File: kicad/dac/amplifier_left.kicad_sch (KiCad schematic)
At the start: 29 parts, among them Q2 PNP, Q3 PNP, Q4 NPN, Q5 NPN, Q6 NPN, Q7 PNP, Q8 NPN, Q9 PNP

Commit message: split power supply to different board
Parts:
- removed HS1: Heatsink_Pad, symbol Mechanical:Heatsink_Pad
- added HS1: Heatsink, Heatsink:Heatsink_Fischer_SK104-STCB_35x13mm__2xDrill3.5mm_ScrewM3, symbol Mechanical:Heatsink
- C12: value 750n -> 1u
- Q4: footprint (none) -> Package_TO_SOT_THT:TO-92L_Inline
- Q8, Q9: footprint (none) -> Package_TO_SOT_THT:TO-220-3_Vertical
- R15: value 1k -> 870
- RV1: footprint (none) -> library:RK09L12B
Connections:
- net IN_L renamed IN
- net OUT_L renamed OUT

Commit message: Commit
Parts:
- removed C12: 1u, symbol Device:C
- removed I1: 2mA, symbol Simulation_SPICE:IDC
- removed I2: 10mA, symbol Simulation_SPICE:IDC
- removed Q2, Q3: PNP, symbol Simulation_SPICE:PNP
- removed Q5: NPN, symbol Simulation_SPICE:NPN
- removed R15: 870, Resistor_THT:R_Axial_DIN0207_L6.3mm_D2.5mm_P10.16mm_Horizontal, symbol Device:R
- removed R19: 22, Resistor_THT:R_Axial_DIN0207_L6.3mm_D2.5mm_P10.16mm_Horizontal, symbol Device:R
- removed R20, R21: 33, Resistor_THT:R_Axial_DIN0207_L6.3mm_D2.5mm_P10.16mm_Horizontal, symbol Device:R
- removed R22, R23: 330m, symbol Device:R
- added C11: 120p, symbol Device:C
- added C20: 10u, Capacitor_THT:CP_Radial_D5.0mm_P2.50mm, symbol Device:C_Polarized
- added C21, C22: 10u, symbol Device:C
- added C23, C24: 100u, symbol Device:C_Polarized
- added Q10: NPN, Package_SO:SC-74-6_1.5x2.9mm_P0.95mm, symbol library:Dual-NPN
- added Q12, Q8: PNP, Package_SO:SC-74-6_1.5x2.9mm_P0.95mm, symbol library:Dual-PNP
- added Q4 (x2): NPN, Package_TO_SOT_THT:TO-92, symbol Simulation_SPICE:NPN
- added unit 2 of Q8
- added unit 2 of Q9
- added R12: 470, Resistor_SMD:R_1206_3216Metric_Pad1.30x1.75mm_HandSolder, symbol Device:R
- added R13: 68, Resistor_THT:R_Axial_DIN0207_L6.3mm_D2.5mm_P10.16mm_Horizontal, symbol Device:R
- added R13 (x2), R15: 68, Resistor_SMD:R_1206_3216Metric_Pad1.30x1.75mm_HandSolder, symbol Device:R
- added R15: 680, Resistor_SMD:R_1206_3216Metric_Pad1.30x1.75mm_HandSolder, symbol Device:R
- added R15 (x2): 27k, Resistor_SMD:R_1206_3216Metric_Pad1.30x1.75mm_HandSolder, symbol Device:R
- added R19: 22, Resistor_SMD:R_1206_3216Metric_Pad1.30x1.75mm_HandSolder, symbol Device:R
- added R19: 2k2, Resistor_SMD:R_1206_3216Metric_Pad1.30x1.75mm_HandSolder, symbol Device:R
- added R20 (x2): 33, Resistor_SMD:R_1206_3216Metric_Pad1.30x1.75mm_HandSolder, symbol Device:R
- added R38: 500, symbol Device:R_Trim
- added R40: 100, Resistor_SMD:R_1206_3216Metric_Pad1.30x1.75mm_HandSolder, symbol Device:R
- added R9 (x2): 1, Resistor_THT:R_Axial_DIN0614_L14.3mm_D5.7mm_P20.32mm_Horizontal, symbol Device:R
- added RV2: 100, symbol Device:R_Potentiometer_Trim
- C10: footprint (none) -> Capacitor_SMD:C_1206_3216Metric_Pad1.33x1.80mm_HandSolder
- C7: value 1n -> 2u2
- HS1: footprint Heatsink:Heatsink_Fischer_SK104-STCB_35x13mm__2xDrill3.5mm_ScrewM3 -> Heatsink:Heatsink_Fischer_SK129-STS_42x25mm_2xDrill2.5mm; Digikey (none) -> HS404-ND; DigikeyAlt (none) -> FA-T220-25E-ND; Height (none) -> 25.4mm
- Q4: footprint Package_TO_SOT_THT:TO-92L_Inline -> Package_TO_SOT_THT:TO-92
- R12: value 1k -> 470; footprint Resistor_THT:R_Axial_DIN0207_L6.3mm_D2.5mm_P10.16mm_Horizontal -> Resistor_SMD:R_1206_3216Metric_Pad1.30x1.75mm_HandSolder
- R13, R14: value 234 -> 430; footprint Resistor_THT:R_Axial_DIN0207_L6.3mm_D2.5mm_P10.16mm_Horizontal -> Resistor_SMD:R_1206_3216Metric_Pad1.30x1.75mm_HandSolder
- R15: value 1k -> 2k
- R16: value 10k -> 20k
- R17: value 1k2 -> 2k2; footprint Resistor_THT:R_Axial_DIN0207_L6.3mm_D2.5mm_P10.16mm_Horizontal -> Resistor_SMD:R_1206_3216Metric_Pad1.30x1.75mm_HandSolder
- R18: value 518 -> 680; footprint Resistor_THT:R_Axial_DIN0207_L6.3mm_D2.5mm_P10.16mm_Horizontal -> Resistor_SMD:R_1206_3216Metric_Pad1.30x1.75mm_HandSolder
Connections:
- net GNDA: now also C11.2, C21.2, C22.1, C23.2, C24.1, Q4.1 (C), R15.1, R15.1
- net IN: now also R13.1; no longer RV1.1
- net OUT: now also R20.1, R20.2, R9.1, R9.2
- net at R12.2: now also Q10.5 (E); no longer C10.1
- net at C10.2, Q4.3 (E), Q7.2 (B): now also C20.2, Q4.1 (C), R38.2; no longer R18.1
- net at R13.2: now also R13.1, RV2.1; no longer R14.1
- net at C7.2, R11.2: now also Q8.1 (B)
- net at R13.1: now also Q8.5 (E)
- net at Q8.3 (E): now also R9.1
- net at Q7.3 (E), Q9.2 (B): now also R20.1
- net at R15.2, R16.1: now also Q8.2 (B)
- net at Q6.3 (E), Q8.2 (B): now also R20.2
- net at R14.2: now also Q8.4 (E)
- net at Q4.1 (C), Q6.2 (B): now also C20.1, R40.2; no longer R17.2
- net at Q9.3 (E): now also R9.2
- net +36V renamed +30V
- net +30V: now also C21.1, C23.1, Q12.5 (E), Q9.5 (E), R15.2, R15.2
- net -36V renamed -30V
- net -30V: now also C22.2, C24.2, R12.1, R19.1, R19.1
- new net: Q12.3 (C), R17.2, R40.1
- new net: R18.1, R38.1
- new net: Q4.2 (B), Q4.3 (E), R19.2
- new net: Q4.3 (E), R19.2
- new net: C11.1, R13.2, RV1.1
- new net: C10.1, Q10.6 (C), Q4.2 (B), Q8.6 (C)
- new net: R13.1, R14.1, RV2.3
- new net: Q10.1 (B), Q10.2 (B), Q10.3 (C), Q8.3 (C)
- new net: Q9.2 (B), Q9.6 (C), R15.2
- new net: Q9.3 (C), R13.2, R13.2, RV2.2
- new net: Q9.1 (B), Q9.4 (E), R15.1
- new net: Q10.4 (E), R12.2
- new net: Q12.2 (B), Q12.6 (C), R15.2
- new net: Q12.1 (B), Q12.4 (E), R15.1
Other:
- note added: "0.5mA"
- note added: "1.7V above V-"
- note added: "10mA"
- note added: "1mA"
- note added: "=Vbe factor * re'"
- note added: "Iq=26mA"
- note added: "MASTER"
- note added: "This sheet for the left channel amplifier is where design changes happen. Afterwards its design is copied to the right channel amplifier. Beware of potentiometer A/B variants. All resistors are 1/4W 1206 unless specified."
- note added: "Vbias=4*Vbe"
- note added: "best transistors: input: ultra low noise, low Cob, well matched vas: first part: fT >> 100MHz @ Ic, low noise vas: last part: fT >> 100MHz @ Ic, small Early effect, low Cob output: first part: low Cob output: last part: big SOA"
- note added: "wire wound: galaxy brain metal thin film: yeah boi carbon film: good metal thick film: meh metal oxide film: trash carbon composition: trash"
- title: USB DAC & Headphone Amplifier -> Left Channel Amplifier
- moved on the sheet: C10, C7, HS1, Q4, R11, R12, R13, R14, R15, R16, R17, R18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

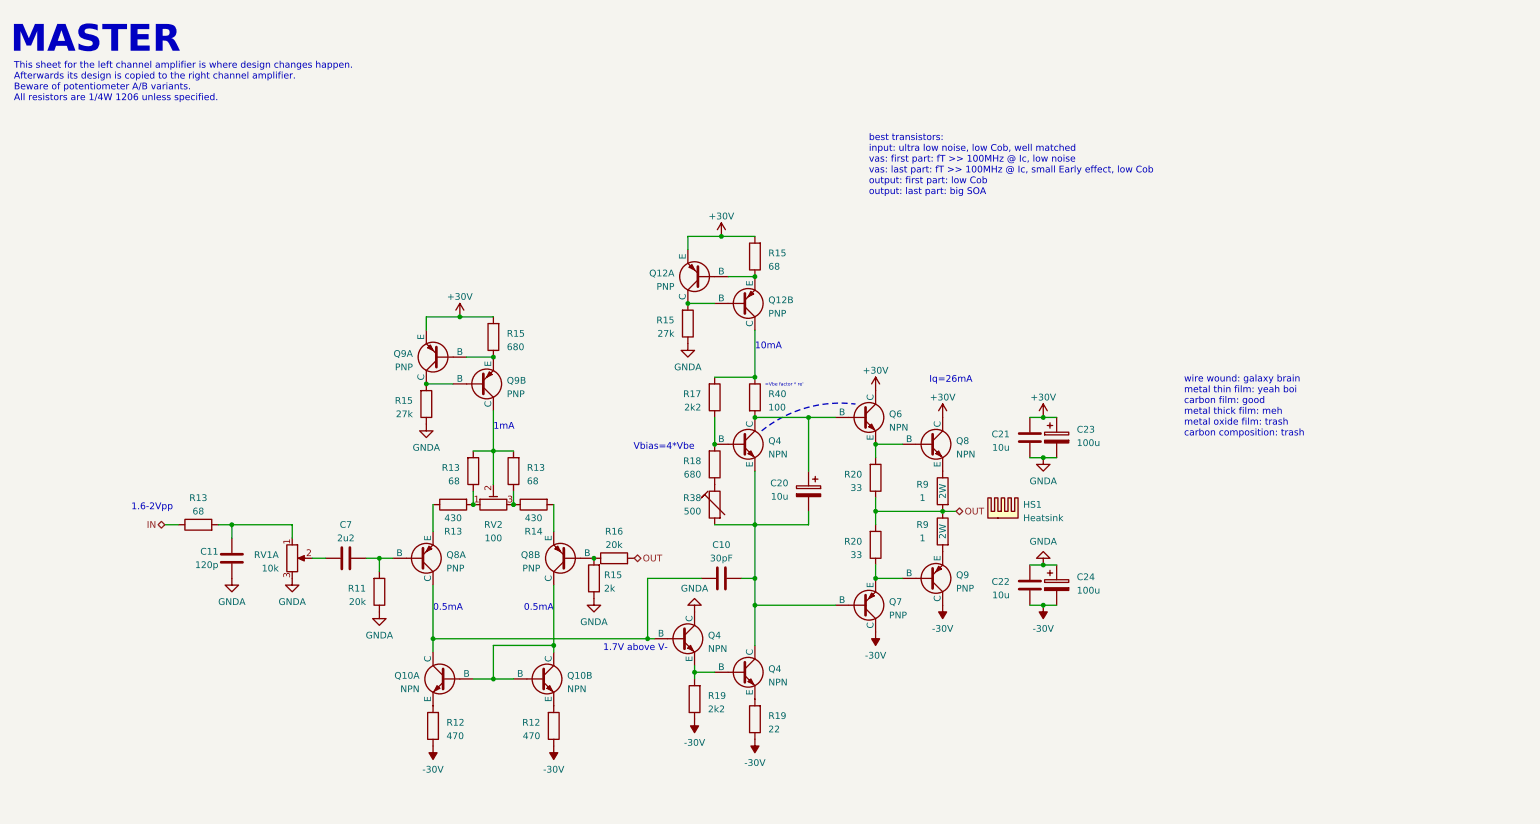
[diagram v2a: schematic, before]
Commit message: completed power supply footprints and placement
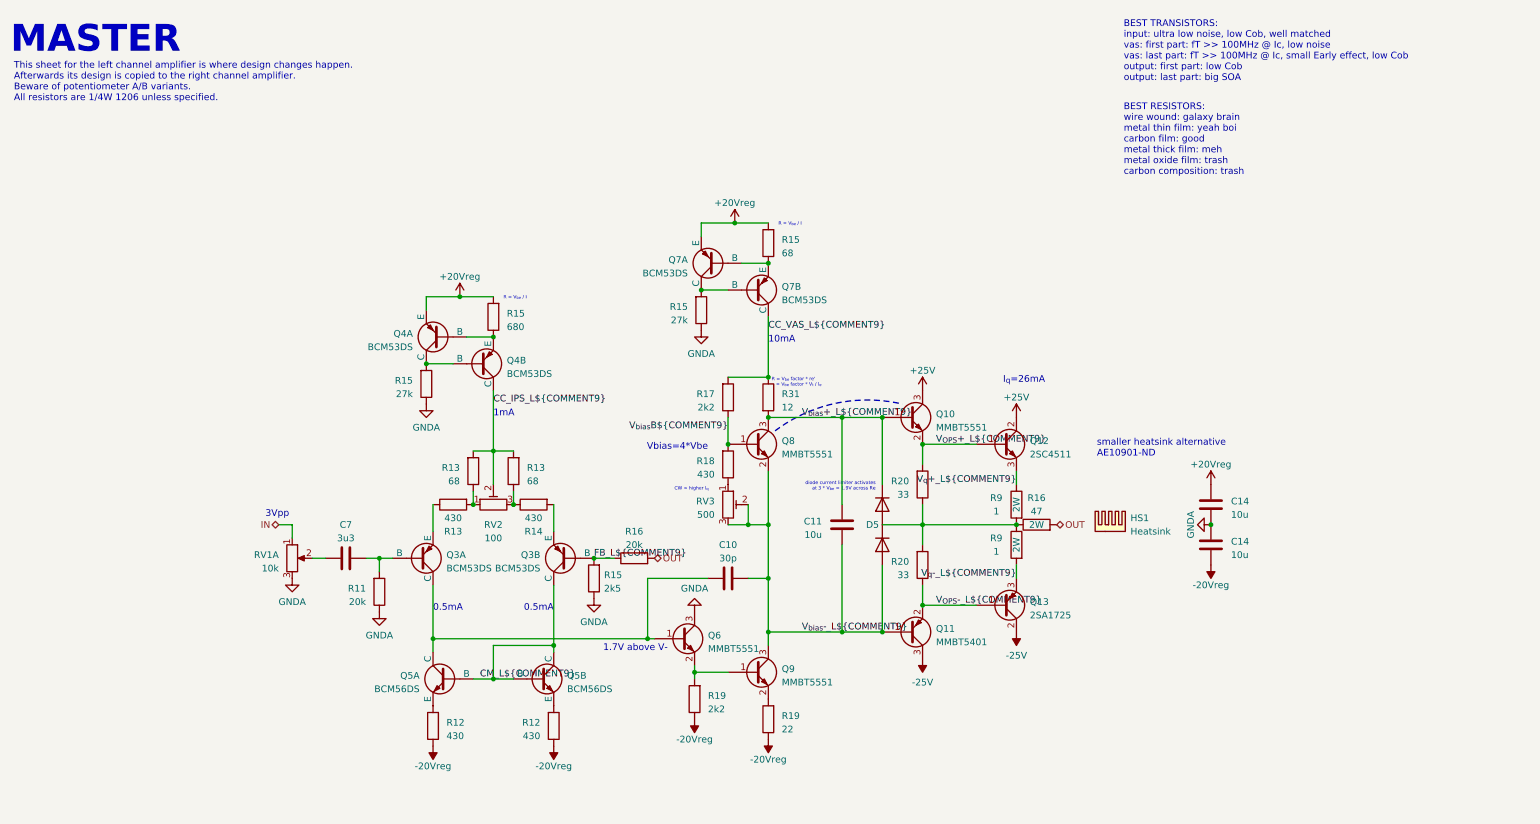
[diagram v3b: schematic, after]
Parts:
- removed C20: 10u, Capacitor_THT:CP_Radial_D5.0mm_P2.50mm, symbol Device:C_Polarized
- removed C21, C22: 10u, symbol Device:C
- removed C23, C24: 100u, symbol Device:C_Polarized
- removed Q4 (x3): NPN, Package_TO_SOT_THT:TO-92, symbol Simulation_SPICE:NPN
- removed Q6: NPN, symbol Simulation_SPICE:NPN
- removed Q7: PNP, symbol Simulation_SPICE:PNP
- removed Q8: NPN, Package_TO_SOT_THT:TO-220-3_Vertical, symbol Simulation_SPICE:NPN
- removed Q9: PNP, Package_TO_SOT_THT:TO-220-3_Vertical, symbol Simulation_SPICE:PNP
- removed R13: 68, Resistor_THT:R_Axial_DIN0207_L6.3mm_D2.5mm_P10.16mm_Horizontal, symbol Device:R
- removed R38: 500, symbol Device:R_Trim
- added C14 (x2): 10u, Capacitor_SMD:C_1206_3216Metric_Pad1.33x1.80mm_HandSolder, symbol Device:C
- added D5: ~, Package_TO_SOT_SMD:SOT-23-3, symbol library:Dual_Diode_Array
- added Q10, Q6, Q8, Q9: MMBT5551, Package_TO_SOT_SMD:SOT-23-3, symbol Device:Q_NPN_BEC
- added Q11: MMBT5401, Package_TO_SOT_SMD:SOT-23-3, symbol Device:Q_PNP_BEC
- added Q12: 2SC4511, Package_TO_SOT_THT:TO-220F-3_Vertical, symbol Device:Q_NPN_BCE
- added Q13: 2SA1725, Package_TO_SOT_THT:TO-220F-3_Vertical, symbol Device:Q_PNP_BCE
- added R16: 47, symbol Device:R
- added RV3: 500, library:TC33, symbol Device:R_Potentiometer_Trim
- C10: value 30pF -> 30p
- C11: value 120p -> 10u; footprint (none) -> Capacitor_SMD:C_1206_3216Metric_Pad1.33x1.80mm_HandSolder; Digikey (none) -> 1276-3100-1-ND
- C7: value 2u2 -> 3u3; footprint (none) -> Capacitor_THT:C_Rect_L7.2mm_W7.2mm_P5.00mm_FKS2_FKP2_MKS2_MKP2; Digikey (none) -> 1928-1645-ND; Height (none) -> 13mm
- Q3: renamed from Q8; value PNP -> BCM53DS
- Q4: renamed from Q9; value PNP -> BCM53DS; footprint Package_SO:TSOP-6_1.65x3.05mm_P0.95mm -> Package_SO:SC-74-6_1.5x2.9mm_P0.95mm
- Q5: renamed from Q10; value NPN -> BCM56DS
- Q7: renamed from Q12; value PNP -> BCM53DS
- R12: value 470 -> 430
- R15: value 2k -> 2k5
- R18: value 680 -> 430
- R31: renamed from R40; value 100 -> 12
- RV2: footprint (none) -> library:TC33; Digikey (none) -> 118-TC33X-2-101GCT-ND
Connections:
- net GNDA: now also C14.1, C14.2, Q6.3 (C); no longer C11.2
- net IN: now also RV1.1
- net OUT: now also R16.2; no longer R20.1, R20.2, R9.1, R9.2
- net CC_VAS${COMMENT8}${COMMENT9}: now reaches Q7.3 (C), R17.2, R31.1
- net V_{bias}+${COMMENT8}${COMMENT9}: now reaches R31.2
- net V_{bias}+${COMMENT8}${COMMENT9}: now also C11.1, D5.2 (C), Q10.1 (B), Q8.3 (C)
- net at R18.1: now also RV3.1
- net V_{bias}B${COMMENT9}: now reaches R17.1, R18.2
- net V_{bias}B${COMMENT9}: now also Q8.1 (B)
- net V_{bias}-${COMMENT8}${COMMENT9}: now reaches C10.2
- net V_{bias}-${COMMENT8}${COMMENT9}: now also C11.2, D5.1 (A), Q11.1 (B), Q8.2 (E), Q9.3 (C), RV3.2, RV3.3
- net at R19.2: now also Q6.2 (E), Q9.1 (B)
- net at R19.2: now also Q9.2 (E)
- net V_{OPS}-${COMMENT8}${COMMENT9}: now reaches R20.1
- net V_{OPS}-${COMMENT8}${COMMENT9}: now also Q11.2 (E), Q13.1 (B)
- net at C10.1, Q3.6 (C), Q5.6 (C): now also Q6.1 (B)
- net FB${COMMENT8}${COMMENT9}: now reaches Q3.2 (B), R15.2, R16.1
- net V_{OPS}+${COMMENT8}${COMMENT9}: now reaches R20.2
- net V_{OPS}+${COMMENT8}${COMMENT9}: now also Q10.2 (E), Q12.1 (B)
- net V_{q}+${COMMENT8}${COMMENT9}: now reaches R9.1
- net V_{q}+${COMMENT8}${COMMENT9}: now also Q12.3 (E)
- net CM${COMMENT8}${COMMENT9}: now reaches Q3.3 (C), Q5.1 (B), Q5.2 (B), Q5.3 (C)
- net V_{q}-${COMMENT8}${COMMENT9}: now reaches R9.2
- net V_{q}-${COMMENT8}${COMMENT9}: now also Q13.3 (E)
- net CC_IPS${COMMENT8}${COMMENT9}: now reaches Q4.3 (C), R13.2, R13.2, RV2.2
- net +30V renamed +20Vreg
- net +20Vreg: now also C14.1
- net -30V renamed -20Vreg
- net -20Vreg: now also C14.2
- new net: D5.3 (C/A), R16.1, R20.1, R20.2, R9.1, R9.2
- new net +25V: Q10.3 (C), Q12.2 (C)
- new net -25V: Q11.3 (C), Q13.2 (C)
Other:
- note added: "3Vpp"
- note added: "BEST RESISTORS: wire wound: galaxy brain metal thin film: yeah boi carbon film: good metal thick film: meh metal oxide film: trash carbon composition: trash"
- note added: "BEST TRANSISTORS: input: ultra low noise, low Cob, well matched vas: first part: fT >> 100MHz @ Ic, low noise vas: last part: fT >> 100MHz @ Ic, small Early effect, low Cob output: first part: low Cob output: last part: big SOA"
- note added: "CW = higher I_{q}"
- note added: "I_{q}=26mA"
- note added: "R = V_{be} / I"
- note added: "R = V_{be} factor * re' = V_{be} factor * V_{t} / I_{e}"
- note added: "diode current limiter activates at 3 * V_{be} = 1.9V across Re"
- note added: "smaller heatsink alternative AE10901-ND"
- note removed: "1.6-2Vpp"
- note removed: "=Vbe factor * re'"
- note removed: "Iq=26mA"
- note removed: "best transistors: input: ultra low noise, low Cob, well matched vas: first part: fT >> 100MHz @ Ic, low noise vas: last part: fT >> 100MHz @ Ic, small Early effect, low Cob output: first part: low Cob output: last part: big SOA"
- note removed: "wire wound: galaxy brain metal thin film: yeah boi carbon film: good metal thick film: meh metal oxide film: trash carbon composition: trash"
- company: (none) -> Author: Jona Heinke
- moved on the sheet: C10, HS1, Q4A, Q4B, Q7A, Q7B, R15, R16, R17, R18, R19, R20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

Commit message: commit
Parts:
- removed C14 (x2): 10u, Capacitor_SMD:C_1206_3216Metric_Pad1.33x1.80mm_HandSolder, symbol Device:C
- removed D5: ~, Package_TO_SOT_SMD:SOT-23-3, symbol library:Dual_Diode_Array
- removed Q10, Q6, Q8, Q9: MMBT5551, Package_TO_SOT_SMD:SOT-23-3, symbol Device:Q_NPN_BEC
- removed Q11: MMBT5401, Package_TO_SOT_SMD:SOT-23-3, symbol Device:Q_PNP_BEC
- removed Q12: 2SC4511, Package_TO_SOT_THT:TO-220F-3_Vertical, symbol Device:Q_NPN_BCE
- removed Q13: 2SA1725, Package_TO_SOT_THT:TO-220F-3_Vertical, symbol Device:Q_PNP_BCE
- removed R12 (x2), R13: 430, Resistor_SMD:R_1206_3216Metric_Pad1.30x1.75mm_HandSolder, symbol Device:R
- removed R13 (x2), R15: 68, Resistor_SMD:R_1206_3216Metric_Pad1.30x1.75mm_HandSolder, symbol Device:R
- removed R15: 2k5, Resistor_THT:R_Axial_DIN0207_L6.3mm_D2.5mm_P10.16mm_Horizontal, symbol Device:R
- removed R15: 680, Resistor_SMD:R_1206_3216Metric_Pad1.30x1.75mm_HandSolder, symbol Device:R
- removed R15 (x2): 27k, Resistor_SMD:R_1206_3216Metric_Pad1.30x1.75mm_HandSolder, symbol Device:R
- removed R16: 47, symbol Device:R
- removed R16: 20k, Resistor_THT:R_Axial_DIN0207_L6.3mm_D2.5mm_P10.16mm_Horizontal, symbol Device:R
- removed R19: 22, Resistor_SMD:R_1206_3216Metric_Pad1.30x1.75mm_HandSolder, symbol Device:R
- removed R19: 2k2, Resistor_SMD:R_1206_3216Metric_Pad1.30x1.75mm_HandSolder, symbol Device:R
- removed R20 (x2): 33, Resistor_SMD:R_1206_3216Metric_Pad1.30x1.75mm_HandSolder, symbol Device:R
- removed R31: 12, Resistor_SMD:R_1206_3216Metric_Pad1.30x1.75mm_HandSolder, symbol Device:R
- removed R9 (x2): 1, Resistor_THT:R_Axial_DIN0614_L14.3mm_D5.7mm_P20.32mm_Horizontal, symbol Device:R
- added C12 (x2): 20n, Capacitor_SMD:C_1206_3216Metric_Pad1.33x1.80mm_HandSolder, symbol Device:C
- added C14 (x4): 10u, Capacitor_SMD:C_1206_3216Metric_Pad1.33x1.80mm_HandSolder, symbol Device:C
- added D9: ~, Package_TO_SOT_SMD:SOT-23-3, symbol Device:D_Dual_Series_ACK
- added Q10: 2SC4511, Package_TO_SOT_THT:TO-220F-3_Vertical, symbol Device:Q_NPN_BCE
- added Q11: 2SA1725, Package_TO_SOT_THT:TO-220F-3_Vertical, symbol Device:Q_PNP_BCE
- added Q6, Q8: BCM56DS, Package_SO:SC-74-6_1.5x2.9mm_P0.95mm, symbol library:Dual-NPN
- added Q9: BCM53DS, Package_SO:SC-74-6_1.5x2.9mm_P0.95mm, symbol library:Dual-PNP
- added R12 (x2), R13: 430, Resistor_SMD:R_1206_3216Metric_Pad1.30x1.75mm_HandSolder, symbol Device:R
- added R13 (x2), R15, R16: 68, Resistor_SMD:R_1206_3216Metric_Pad1.30x1.75mm_HandSolder, symbol Device:R
- added R15 (x2), R16: 27k, Resistor_SMD:R_1206_3216Metric_Pad1.30x1.75mm_HandSolder, symbol Device:R
- added R15: 680, Resistor_SMD:R_1206_3216Metric_Pad1.30x1.75mm_HandSolder, symbol Device:R
- added R15, R19: 2k2, Resistor_SMD:R_1206_3216Metric_Pad1.30x1.75mm_HandSolder, symbol Device:R
- added R19: 22, Resistor_SMD:R_1206_3216Metric_Pad1.30x1.75mm_HandSolder, symbol Device:R
- added R2: 16, Resistor_SMD:R_1206_3216Metric_Pad1.30x1.75mm_HandSolder, symbol Device:R
- added R20 (x2): 33, Resistor_SMD:R_1206_3216Metric_Pad1.30x1.75mm_HandSolder, symbol Device:R
- added R30: 12, Resistor_SMD:R_1206_3216Metric_Pad1.30x1.75mm_HandSolder, symbol Device:R
- added R9 (x2): 2, Resistor_THT:R_Axial_DIN0614_L14.3mm_D5.7mm_P20.32mm_Horizontal, symbol Device:R
- R11: value 20k -> 27k; footprint Resistor_THT:R_Axial_DIN0207_L6.3mm_D2.5mm_P10.16mm_Horizontal -> Resistor_SMD:R_1206_3216Metric_Pad1.30x1.75mm_HandSolder
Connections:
- net +20Vreg: now also C14.1, C14.1, R15.2, R15.2
- net +25V: now also Q10.2 (C), Q8.3 (C)
- net -20Vreg: now also C14.1, C14.1, R12.1, R12.1, R19.1, R19.1
- net -25V: now also Q11.2 (C), Q9.2 (B), Q9.3 (C), Q9.4 (E), Q9.6 (C)
- net GNDA: now also C12.1, C12.1, C14.2, C14.2, C14.2, C14.2, Q6.6 (C), R15.1, R15.1, R15.1
- net IN: now also R16.1; no longer RV1.1
- net OUT: now also D9.2 (common), R16.2, R2.2, R20.1, R20.2, R9.1, R9.2
- net at Q5.5 (E): now also R12.2
- net at C7.1: now also C12.2, R16.2; no longer RV1.2
- net INPUT_L: now reaches Q3.1 (B), R11.2
- net INPUT_L: now also RV1.2; no longer C7.2
- net at Q3.5 (E): now also R13.1
- net at RV2.1: now also R13.1, R13.2
- net at R14.1, RV2.3: now also R13.1
- net IPS_L: now reaches C10.1, Q3.6 (C), Q5.6 (C)
- net IPS_L: now also Q6.1 (B)
- net at Q4.2 (B), Q4.6 (C): now also R15.2
- net at Q4.1 (B), Q4.4 (E): now also R15.1
- net at Q5.4 (E): now also R12.2
- net at Q7.2 (B), Q7.6 (C): now also R15.2
- net at Q7.1 (B), Q7.4 (E): now also R15.1
- net CC_IPS${COMMENT8}${COMMENT9} renamed CC_IPS_L
- net CC_IPS_L: now also R13.2, R13.2
- net CC_VAS${COMMENT8}${COMMENT9} renamed CC_VAS_L
- net CC_VAS_L: now also R30.1
- net CM${COMMENT8}${COMMENT9} renamed CM_L
- net FB${COMMENT8}${COMMENT9} renamed FB_L
- net FB_L: now also R15.2, R16.1
- net V_{bias}+${COMMENT8}${COMMENT9} renamed V_{bias}+_L
- net V_{bias}+_L: now also D9.3 (K), Q8.2 (B), Q8.6 (C), R30.2
- net V_{bias}-${COMMENT8}${COMMENT9} renamed V_{bias}-_L
- net V_{bias}-_L: now also D9.1 (A), Q6.3 (C), Q8.5 (E), Q9.1 (B)
- net V_{bias}B${COMMENT9} renamed V_{bias}B_L
- net V_{bias}B_L: now also Q8.1 (B)
- new net: C7.2, RV1.1
- new net: Q6.4 (E), R19.2
- new net VAS_DARL_L: Q6.2 (B), Q6.5 (E), R19.2
- new net V_{OPS}+_L: Q10.1 (B), Q8.4 (E), R20.2
- new net V_{OPS}-_L: Q11.1 (B), Q9.5 (E), R20.1
- new net V_{q}+_L: Q10.3 (E), R9.1
- new net V_{q}-_L: Q11.3 (E), R9.2
- new net ZOBEL_L: C12.2, R2.1
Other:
- note added: "6.6Hz < f < 117kHz"
- note added: "BEST TRANSISTORS: input: ultra low noise, low Cob, well matched vas: first part: fT >> 100MHz @ Ic, low noise vas: last part: fT >> 100MHz @ Ic, small Early effect, low Cob output: first part: low Cob output: last part: big SOA, choose package for heat sink BEST RESISTORS: wire wound: galaxy brain metal thin film: yeah boi carbon film: good metal thick film: meh metal oxide film: trash carbon com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"
- note added: "DC = ½ DAC VA AC < 3Vpp = 1Vrms"
- note added: "I_{q}=13mA"
- note added: "Input Filter"
- note added: "Input Stage"
- note added: "Output Stage"
- note added: "Voltage Amplification Stage"
- note removed: "3Vpp"
- note removed: "BEST RESISTORS: wire wound: galaxy brain metal thin film: yeah boi carbon film: good metal thick film: meh metal oxide film: trash carbon composition: trash"
- note removed: "BEST TRANSISTORS: input: ultra low noise, low Cob, well matched vas: first part: fT >> 100MHz @ Ic, low noise vas: last part: fT >> 100MHz @ Ic, small Early effect, low Cob output: first part: low Cob output: last part: big SOA"
- note removed: "I_{q}=26mA"
- moved on the sheet: RV1A

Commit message: commit
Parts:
- renumbered R30 to R34
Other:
- note added: "DC = ½ DAC VA = 2.5V AC < 3Vpp = 1Vrms"
- note added: "not used"
- note removed: "DC = ½ DAC VA AC < 3Vpp = 1Vrms"
- moved on the sheet: C11, C12, C14, D9, HS1, Q10, Q11, Q6B, Q7A, Q7B, Q8A, Q8B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
